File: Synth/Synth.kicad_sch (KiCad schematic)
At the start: 0 parts

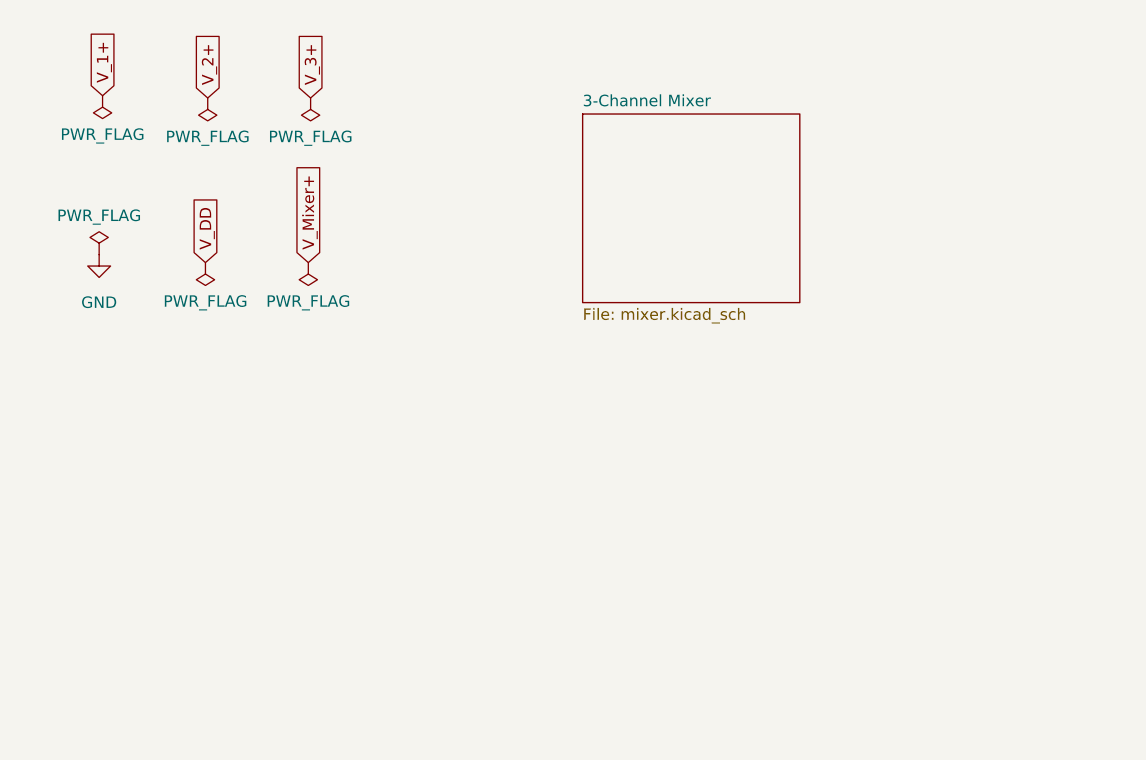
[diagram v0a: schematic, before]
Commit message: added in double wavefolder
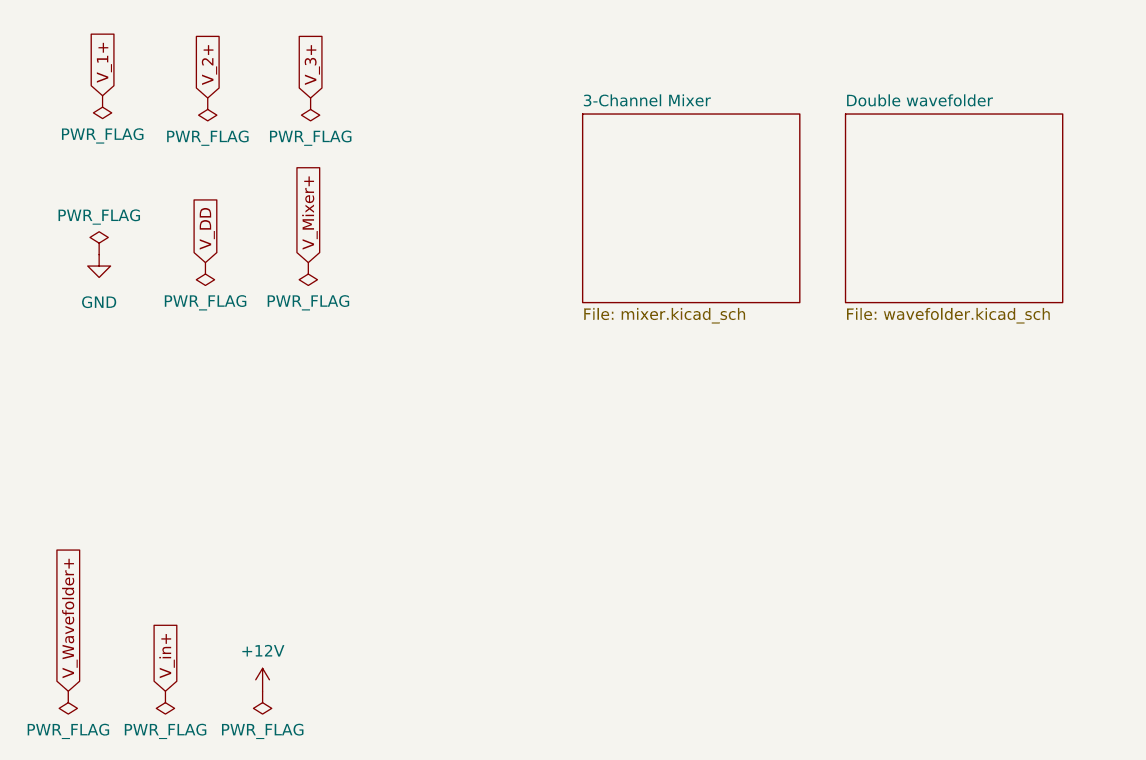
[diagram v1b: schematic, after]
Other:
- added sheet Double wavefolder (wavefolder.kicad_sch)
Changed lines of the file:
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@@
 (kicad_sch (version 20230121) (generator eeschema)
   (paper "A4")
+  (global_label "V_in+" (shape input) (at 29.21 89.535 90) (fields_autoplaced)
+    (effects (font (size 1.27 1.27)) (justify left))
+    (property "Intersheetrefs" "${INTERSHEET_REFS}" (at 29.21 81.1674 90)
+      (effects (font (size 1.27 1.27)) (justify left) hide)
+    )
+  )
   (global_label "V_3+" (shape input) (at 45.339 23.622 90) (fields_autoplaced)
     (effects (font (size 1.27 1.27)) (justify left))
@@
     )
   )
+  (global_label "V_Wavefolder+" (shape input) (at 18.415 89.535 90) (fields_autoplaced)
+    (effects (font (size 1.27 1.27)) (justify left))
+    (property "Intersheetrefs" "${INTERSHEET_REFS}" (at 18.415 72.7009 90)
+      (effects (font (size 1.27 1.27)) (justify left) hide)
+    )
+  )
   (global_label "V_1+" (shape input) (at 22.225 23.368 90) (fields_autoplaced)
     (effects (font (size 1.27 1.27)) (justify left))
@@
     )
   )
+  (symbol (lib_id "power:PWR_FLAG") (at 40.005 89.535 180) (unit 1)
+    (in_bom yes) (on_board yes) (dnp no) (fields_autoplaced)
+    (property "Reference" "#FLG09" (at 40.005 91.44 0)
+      (effects (font (size 1.27 1.27)) hide)
+    )
+    (property "Value" "PWR_FLAG" (at 40.005 93.853 0)
+      (effects (font (size 1.27 1.27)))
+    )
+    (property "Footprint" "" (at 40.005 89.535 0)
+      (effects (font (size 1.27 1.27)) hide)
+    )
+    (property "Datasheet" "~" (at 40.005 89.535 0)
+      (effects (font (size 1.27 1.27)) hide)
+    )
+    (pin "1")
+    (instances
+      (project "Synth"
+        (path "/69caad27-d98a-4cdc-abd0-794bd5e6ba79"
+          (reference "#FLG09") (unit 1)
+        )
+      )
+    )
+  )
   (symbol (lib_id "power:PWR_FLAG") (at 22.225 23.368 180) (unit 1)
     (in_bom yes) (on_board yes) (dnp no) (fields_autoplaced)
@@
     )
   )
+  (symbol (lib_id "power:+12V") (at 40.005 89.535 0) (unit 1)
+    (in_bom yes) (on_board yes) (dnp no) (fields_autoplaced)
+    (property "Reference" "#PWR011" (at 40.005 93.345 0)
+      (effects (font (size 1.27 1.27)) hide)
+    )
+    (property "Value" "+12V" (at 40.005 85.09 0)
+      (effects (font (size 1.27 1.27)))
+    )
+    (property "Footprint" "" (at 40.005 89.535 0)
+      (effects (font (size 1.27 1.27)) hide)
+    )
+    (property "Datasheet" "" (at 40.005 89.535 0)
+      (effects (font (size 1.27 1.27)) hide)
+    )
+    (pin "1")
+    (instances
+      (project "Synth"
+        (path "/69caad27-d98a-4cdc-abd0-794bd5e6ba79"
+          (reference "#PWR011") (unit 1)
+        )
+      )
+    )
+  )
+  (symbol (lib_id "power:PWR_FLAG") (at 29.21 89.535 180) (unit 1)
+    (in_bom yes) (on_board yes) (dnp no) (fields_autoplaced)
+    (property "Reference" "#FLG07" (at 29.21 91.44 0)
+      (effects (font (size 1.27 1.27)) hide)
+    )
+    (property "Value" "PWR_FLAG" (at 29.21 93.853 0)
+      (effects (font (size 1.27 1.27)))
+    )
+    (property "Footprint" "" (at 29.21 89.535 0)
+      (effects (font (size 1.27 1.27)) hide)
+    )
+    (property "Datasheet" "~" (at 29.21 89.535 0)
+      (effects (font (size 1.27 1.27)) hide)
+    )
+    (pin "1")
+    (instances
+      (project "Synth"
+        (path "/69caad27-d98a-4cdc-abd0-794bd5e6ba79"
+          (reference "#FLG07") (unit 1)
+        )
+      )
+    )
+  )
   (symbol (lib_id "power:PWR_FLAG") (at 33.655 41.91 180) (unit 1)
     (in_bom yes) (on_board yes) (dnp no) (fields_autoplaced)
@@
     )
   )
+  (symbol (lib_id "power:PWR_FLAG") (at 18.415 89.535 180) (unit 1)
+    (in_bom yes) (on_board yes) (dnp no) (fields_autoplaced)
+    (property "Reference" "#FLG08" (at 18.415 91.44 0)
+      (effects (font (size 1.27 1.27)) hide)
+    )
+    (property "Value" "PWR_FLAG" (at 18.415 93.853 0)
+      (effects (font (size 1.27 1.27)))
+    )
+    (property "Footprint" "" (at 18.415 89.535 0)
+      (effects (font (size 1.27 1.27)) hide)
+    )
+    (property "Datasheet" "~" (at 18.415 89.535 0)
+      (effects (font (size 1.27 1.27)) hide)
+    )
+    (pin "1")
+    (instances
+      (project "Synth"
+        (path "/69caad27-d98a-4cdc-abd0-794bd5e6ba79"
+          (reference "#FLG08") (unit 1)
+        )
+      )
+    )
+  )
   (symbol (lib_id "power:PWR_FLAG") (at 33.909 23.622 180) (unit 1)
     (in_bom yes) (on_board yes) (dnp no) (fields_autoplaced)
@@
       )
     )
+  )
+  (sheet (at 104.775 25.4) (size 24.13 20.955) (fields_autoplaced)
+    (stroke (width 0.1524) (type solid))
+    (fill (color 0 0 0 0.0000))
+    (property "Sheetname" "Double wavefolder" (at 104.775 24.6884 0)
+      (effects (font (size 1.27 1.27)) (justify left bottom))
+    )
+    (property "Sheetfile" "wavefolder.kicad_sch" (at 104.775 46.9396 0)
+      (effects (font (size 1.27 1.27)) (justify left top))
+    )
+    (instances
+      (project "Synth"
+        (path "/69caad27-d98a-4cdc-abd0-794bd5e6ba79" (page "3"))
+      )
+    )

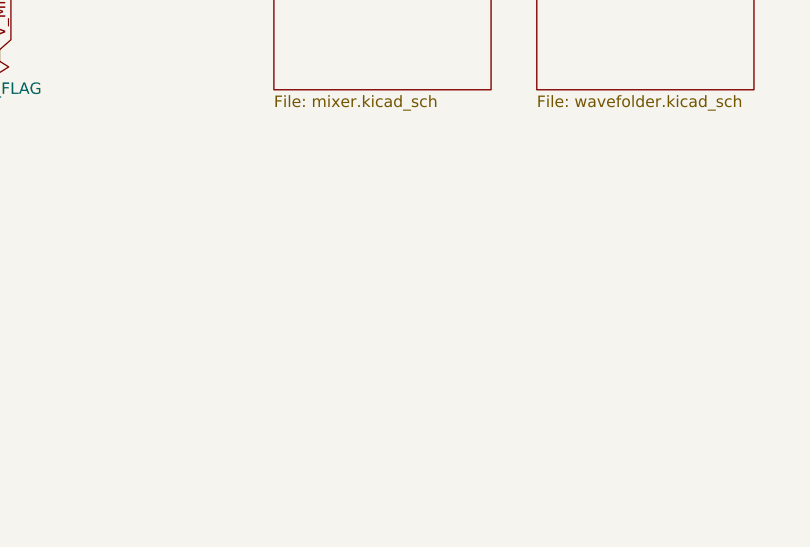
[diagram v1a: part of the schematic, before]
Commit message: merged to the same file
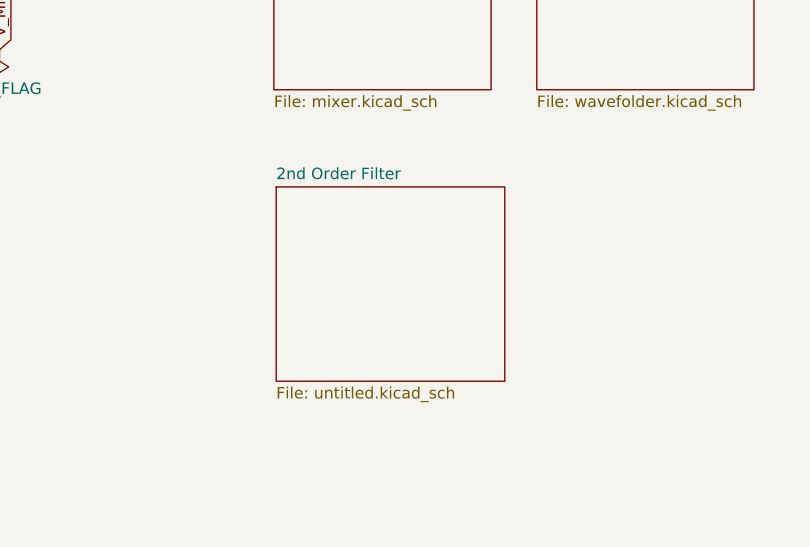
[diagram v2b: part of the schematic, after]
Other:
- added sheet 2nd Order Filter (untitled.kicad_sch)
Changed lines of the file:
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@@
+    )
+  )
+  (sheet (at 75.819 57.15) (size 25.4 21.59) (fields_autoplaced)
+    (stroke (width 0.1524) (type solid))
+    (fill (color 0 0 0 0.0000))
+    (property "Sheetname" "2nd Order Filter" (at 75.819 56.4384 0)
+      (effects (font (size 1.27 1.27)) (justify left bottom))
+    )
+    (property "Sheetfile" "untitled.kicad_sch" (at 75.819 79.3246 0)
+      (effects (font (size 1.27 1.27)) (justify left top))
+    )
+    (instances
+      (project "Synth"
+        (path "/69caad27-d98a-4cdc-abd0-794bd5e6ba79" (page "4"))
+      )
     )
   )

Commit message: fixed erge stuff fingers crossed
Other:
- added sheet 'ADSR' Envelope (envelope.kicad_sch)

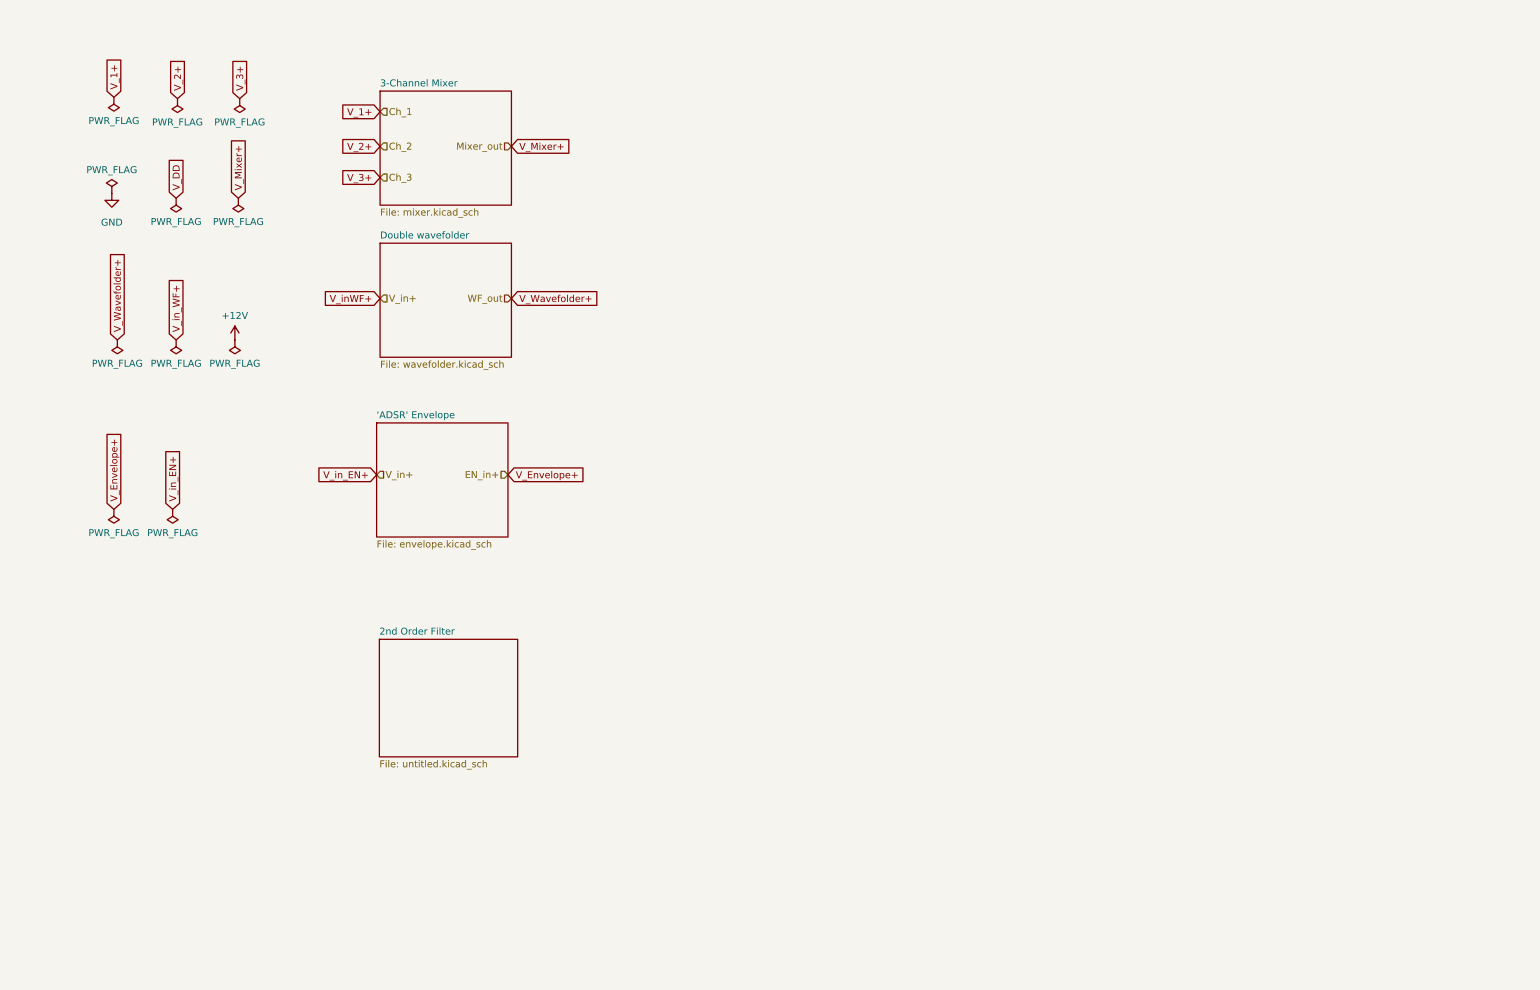
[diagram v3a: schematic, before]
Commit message: removed mixer
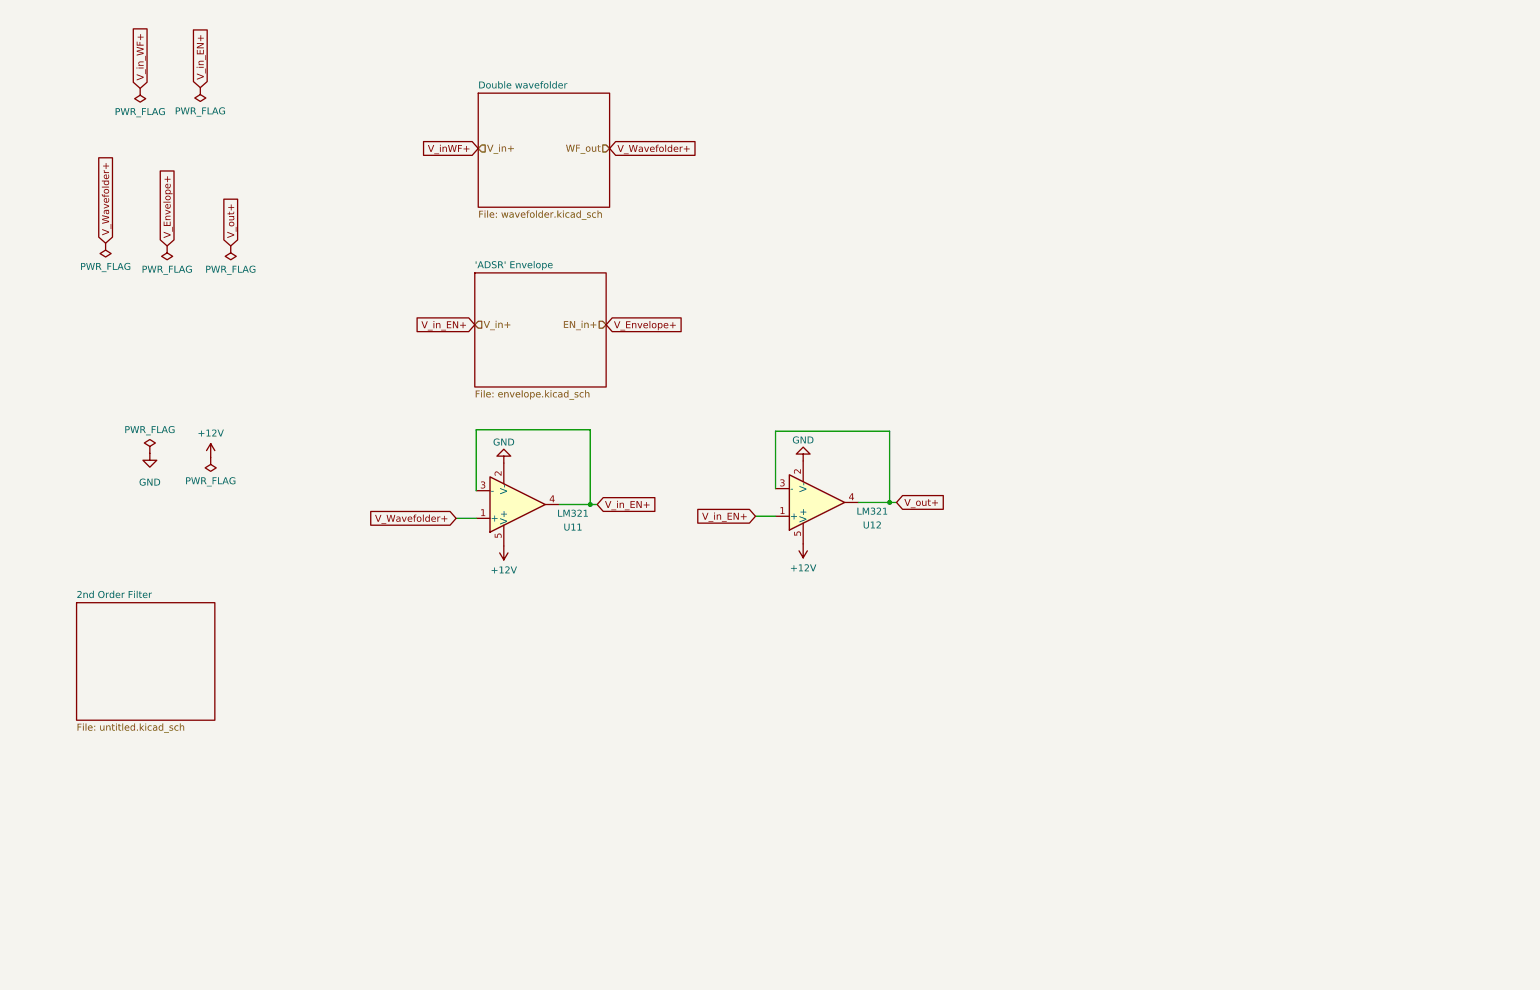
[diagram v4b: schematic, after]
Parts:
- added U11, U12: LM321, Package_TO_SOT_SMD:SOT-23-5, symbol Amplifier_Operational:LM321
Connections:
- net +12V: now also U11.5 (V+), U12.5 (V+)
- net GND: now also U11.2 (V-), U12.2 (V-)
- net V_Wavefolder+: now also U11.1 (+)
- net V_inWF+: now also U11.3 (-), U11.4, U12.1 (+)
- new net V_out+: U12.3 (-), U12.4
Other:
- removed sheet 3-Channel Mixer

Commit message: add the layout
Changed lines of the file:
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@@
+    (stroke (width 0) (type default))
+  )
+  (wire (pts (xy 120.777 72.39) (xy 120.65 72.39))
     (stroke (width 0) (type default))
   )
@@
     )
   )
-  (global_label "V_Envelope+" (shape input) (at 120.65 72.39 0) (fields_autoplaced)
+  (global_label "V_Envelope+" (shape input) (at 120.777 72.39 0) (fields_autoplaced)
     (effects (font (size 1.27 1.27)) (justify left))
-    (property "Intersheetrefs" "${INTERSHEET_REFS}" (at 135.6698 72.39 0)
+    (property "Intersheetrefs" "${INTERSHEET_REFS}" (at 135.7968 72.39 0)
       (effects (font (size 1.27 1.27)) (justify left) hide)
     )
